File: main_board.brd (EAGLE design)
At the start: 100 x 80 mm, 107 parts, among them IC1 MBED_MICROCONTROLLER, U1 PCA9555PW,118, U11 MC33887-HSOP, U13 MC33887-HSOP, U2 SI8460AA-B-IS1, U3 MC33887-HSOP, U6 SI8460AA-B-IS1, U7 MC33887-HSOP, U8 SI8460AA-B-IS1, U9 MC33887-HSOP, X1 BALL_SENS, X10 IMU, X2 ETH, X3 ENC1, X4 ENC2, X5 BTNS, X6 ENC3, X7 ENC4, X8 ENC5, X9 COIL

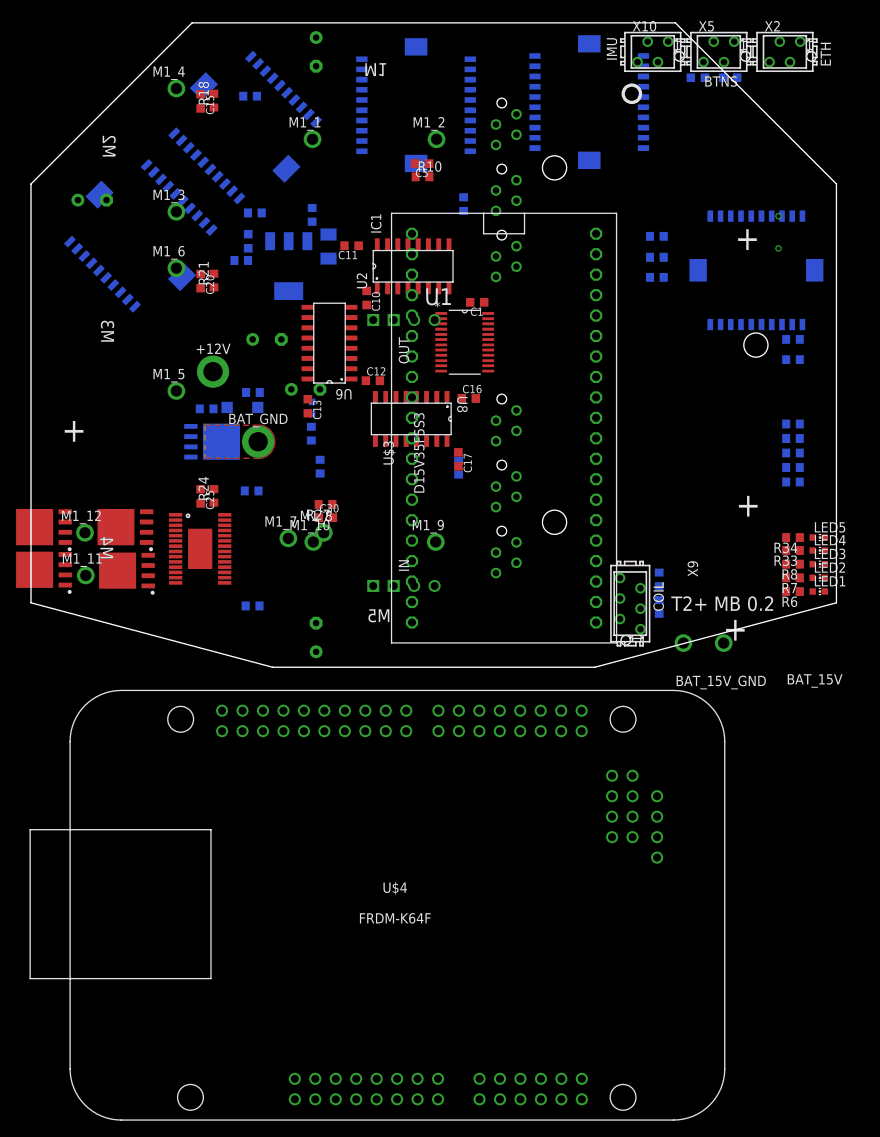
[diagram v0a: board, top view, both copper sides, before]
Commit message: Added one driver module
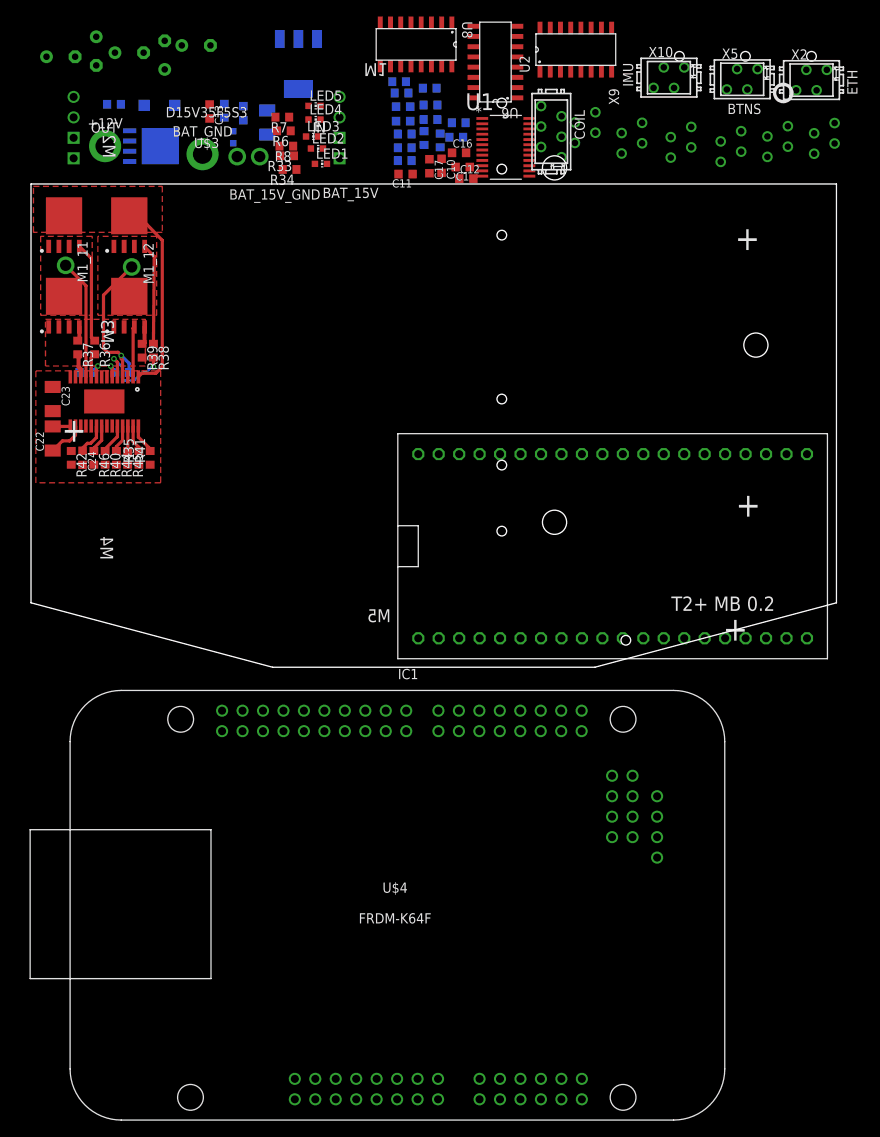
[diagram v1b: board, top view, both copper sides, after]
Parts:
- removed C15, C20, C25, C30, C5: 33nF, rcl:C0603K
- removed M1_1, M1_10, M1_2, M1_3, M1_4, M1_5, M1_6, M1_7, M1_8, M1_9: (no value), tellis2:WIRE_HOLE
- removed R1, R10, R12, R18, R2, R20, R21, R23, R24, R26, R27, R29, R3, R4, R5: 10k, rcl:R0603
- removed U11, U13, U3, U7, U9: MC33887-HSOP, mc33887:HSOP
- added C19, C21, C24: 100nF, rcl:C0603K
- added C22: 470nF, rcl:C1206K
- added C23: 4.7nF, rcl:C1206K
- added R35, R40, R41, R42, R44, R45, R46: 33k, rcl:R0603
- added R36, R37, R38, R39: 47, rcl:R0603
- moved R7 85.4 mm to (31.2, 68.3)
- moved R6 85.2 mm to (31.4, 66.6)
- moved BAT_15V 83.5 mm to (28.4, 63.4)
- moved LED5 82.4 mm to (35.2, 69.7)
- moved LED4 82.3 mm to (35.2, 68.0)
- moved LED3 82.3 mm to (34.9, 65.9)
- moved LED2 82.0 mm to (35.5, 64.4)
- moved BAT_15V_GND 82.0 mm to (25.6, 63.4)
- moved R8 81.5 mm to (31.7, 64.7)
- moved LED1 81.5 mm to (36.0, 62.5)
- moved R33 79.7 mm to (31.8, 63.5)
- moved R34 77.4 mm to (32.1, 61.8)
- moved C9 74.7 mm to (16.6, 76.0)
- moved R19 68.5 mm to (46.0, 71.3)
- moved R22 68.5 mm to (45.7, 72.7)
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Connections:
- removed net CP1: U$5.16
- removed net CP2: U$5.15
- removed net FAUL1T_D: R12.1, U3.2
- removed net FAULT1_D: R20.1, U7.2
- removed net FAULT3_D: R23.1, U9.2
- removed net FAULT4_D: R26.1, U11.2
- removed net FAULT5_D: R29.1, U13.2
- removed net GND_PAD: U$5.PAD
- removed net N$15: C5.1, U3.17
- removed net N$18: R10.2, U3.18
- removed net N$2: R1.1, U3.20
- removed net N$23: M1_1.P$1, U3.6, U3.7
- removed net N$25: M1_2.P$1, U3.14, U3.15
- removed net N$3: R2.1, U7.20
- removed net N$31: C15.1, U7.17
- removed net N$33: R18.2, U7.18
- removed net N$34: M1_3.P$1, U7.6, U7.7
- removed net N$35: M1_4.P$1, U7.14, U7.15
- removed net N$36: C20.1, U9.17
- removed net N$38: R21.2, U9.18
- removed net N$39: M1_5.P$1, U9.6, U9.7
- removed net N$4: R3.1, U13.20
- removed net N$40: M1_6.P$1, U9.14, U9.15
- removed net N$41: C25.1, U11.17
- removed net N$43: R24.2, U11.18
- removed net N$44: M1_7.P$1, U11.6, U11.7
- removed net N$45: M1_8.P$1, U11.14, U11.15
- removed net N$46: C30.1, U13.17
- removed net N$48: R27.2, U13.18
- removed net N$49: M1_9.P$1, U13.6, U13.7
- removed net N$5: R4.1, U11.20
- removed net N$50: M1_10.P$1, U13.14, U13.15
- removed net N$6: R5.1, U9.20
- removed net V5: U$5.20
- removed net VBB: U$5.13, U$5.14
- removed net VREG: U$5.7, U$5.8
- new net DIR1_D: U$5.19
- new net N$19: C21.1, U$5.6
- new net N$26: C19.1, U$5.9
- new net N$27: R35.2, U$5.27
- new net N$28: R36.2, U$5.10
- new net N$29: R38.2, U$5.5
- new net N$30: R37.2, U$5.12
- new net N$32: R39.2, U$5.3
- new net N$37: C22.1, U$5.16
- new net N$42: C22.2, U$5.15
- new net N$47: C23.1, U$5.7, U$5.8
- new net N$51: R41.2, R42.2, U$5.28
- new net N$52: C24.1, R42.1, R44.2, R45.2, R46.2, U$5.20
- new net N$53: R45.1, U$5.26
- new net N$54: R40.1, U$5.24
- new net N$55: R44.1, U$5.25
- new net N$59: R46.1, U$5.21
- net +12V: now also R40.2, U$5.13, U$5.14; no longer U11.16, U11.4, U11.5, U13.16, U13.4, U13.5, U3.16, U3.4, U3.5, U7.16, U7.4, U7.5, U9.16, U9.4, U9.5
- net +5V: no longer R1.2, R12.2, R2.2, R20.2, R23.2, R26.2, R29.2, R3.2, R4.2, R5.2
- net DIR1_1_D: no longer U3.3
- net DIR1_2_D: no longer U3.19
- net DIR2_1_D: no longer U7.3
- net DIR2_2_D: no longer U7.19
- net DIR3_1_D: no longer U9.3
- net DIR3_2_D: no longer U9.19
- net DIR4_1_D: no longer U11.3
- net DIR4_2_D: no longer U11.19
- net DIR5_1_D: no longer U13.3
- net DIR5_2_D: no longer U13.19
- net GND: no longer U$5.17, U$5.18
- net GNDA: now also C23.2, C24.2, R35.1, R41.1, U$5.17, U$5.18, U$5.PAD; no longer C15.2, C20.2, C25.2, C30.2, C5.2, R10.1, R18.1, R21.1, R24.1, R27.1, U11.1, U11.10, U11.11, U11.12, U11.9, U11.SL1, U11.SL2, U13.1, U13.10, U13.11, U13.12, U13.9, U13.SL1, U13.SL2, U3.1, U3.10, U3.11, U3.12, U3.9, U3.SL1, U3.SL2, U7.1, U7.10, U7.11, U7.12, U7.9, U7.SL1, U7.SL2, U9.1, U9.10, U9.11, U9.12, U9.9, U9.SL1, U9.SL2
- net N$13: now also R37.1, U$8.4; no longer U$5.10, U$6.4
- net N$14: now also R38.1; no longer U$5.5
- net N$16: now also R39.1, U$9.4; no longer U$5.12, U$8.4
- net N$17: now also R36.1, U$6.4; no longer U$5.3, U$9.4
- net N$22: now also C19.2
- net N$24: now also C21.2
- net PWM1_D: now also U$5.22, U$5.23; no longer U3.13
- net PWM2_D: no longer U7.13
- net PWM3_D: no longer U9.13
- net PWM4_D: no longer U11.13
- net PWM5_D: no longer U13.13
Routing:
- net +12V: track 0.00 -> 24.6 mm
- net N$24: track 0.00 -> 19.3 mm, vias 0 -> 1
- net N$22: track 0.00 -> 14.9 mm
- net N$14: track 0.00 -> 12.6 mm
- net N$17: track 0.00 -> 12.5 mm
- net N$29: track 0.00 -> 11.1 mm, vias 0 -> 2
- net GNDA: track 0.00 -> 6.27 mm
- net N$37: track 0.00 -> 4.75 mm
- net N$52: track 0.00 -> 4.02 mm
- net N$54: track 0.00 -> 3.73 mm
- net N$51: track 0.00 -> 3.71 mm
- net N$59: track 0.00 -> 3.50 mm
- net N$55: track 0.00 -> 3.42 mm
- net N$27: track 0.00 -> 3.40 mm
- net N$53: track 0.00 -> 3.11 mm
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- added copper zone on layer 1, net +12V
- added copper zone on layer 1, net GNDA
- added copper zone on layer 1, net N$22
- added copper zone on layer 1, net N$24
- removed copper zone on layer 1, net N$21
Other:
- board size 100 x 80 mm -> 100 x 60 mm
